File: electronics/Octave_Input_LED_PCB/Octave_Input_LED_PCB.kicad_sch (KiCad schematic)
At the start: 58 parts, among them J1 HRO_TYPE-C-31-M-12, J2 Conn_01x12, J3 Conn_01x12, SW1 SW_Hot_Swap_Socket, SW10 SW_Hot_Swap_Socket, SW11 SW_Hot_Swap_Socket, SW12 SW_Hot_Swap_Socket, SW2 SW_Hot_Swap_Socket, SW21 Alps_Alpine_SKRP, SW22 Alps_Alpine_SKRP, SW3 SW_Hot_Swap_Socket, SW4 SW_Hot_Swap_Socket, SW5 SW_Hot_Swap_Socket, SW6 SW_Hot_Swap_Socket, SW7 SW_Hot_Swap_Socket, SW8 SW_Hot_Swap_Socket, SW9 SW_Hot_Swap_Socket, U1 AP2112K-3.3, U2 Raspberry_Pi_RP2040, U3 W25Q64JVSS, Y1 12MHz

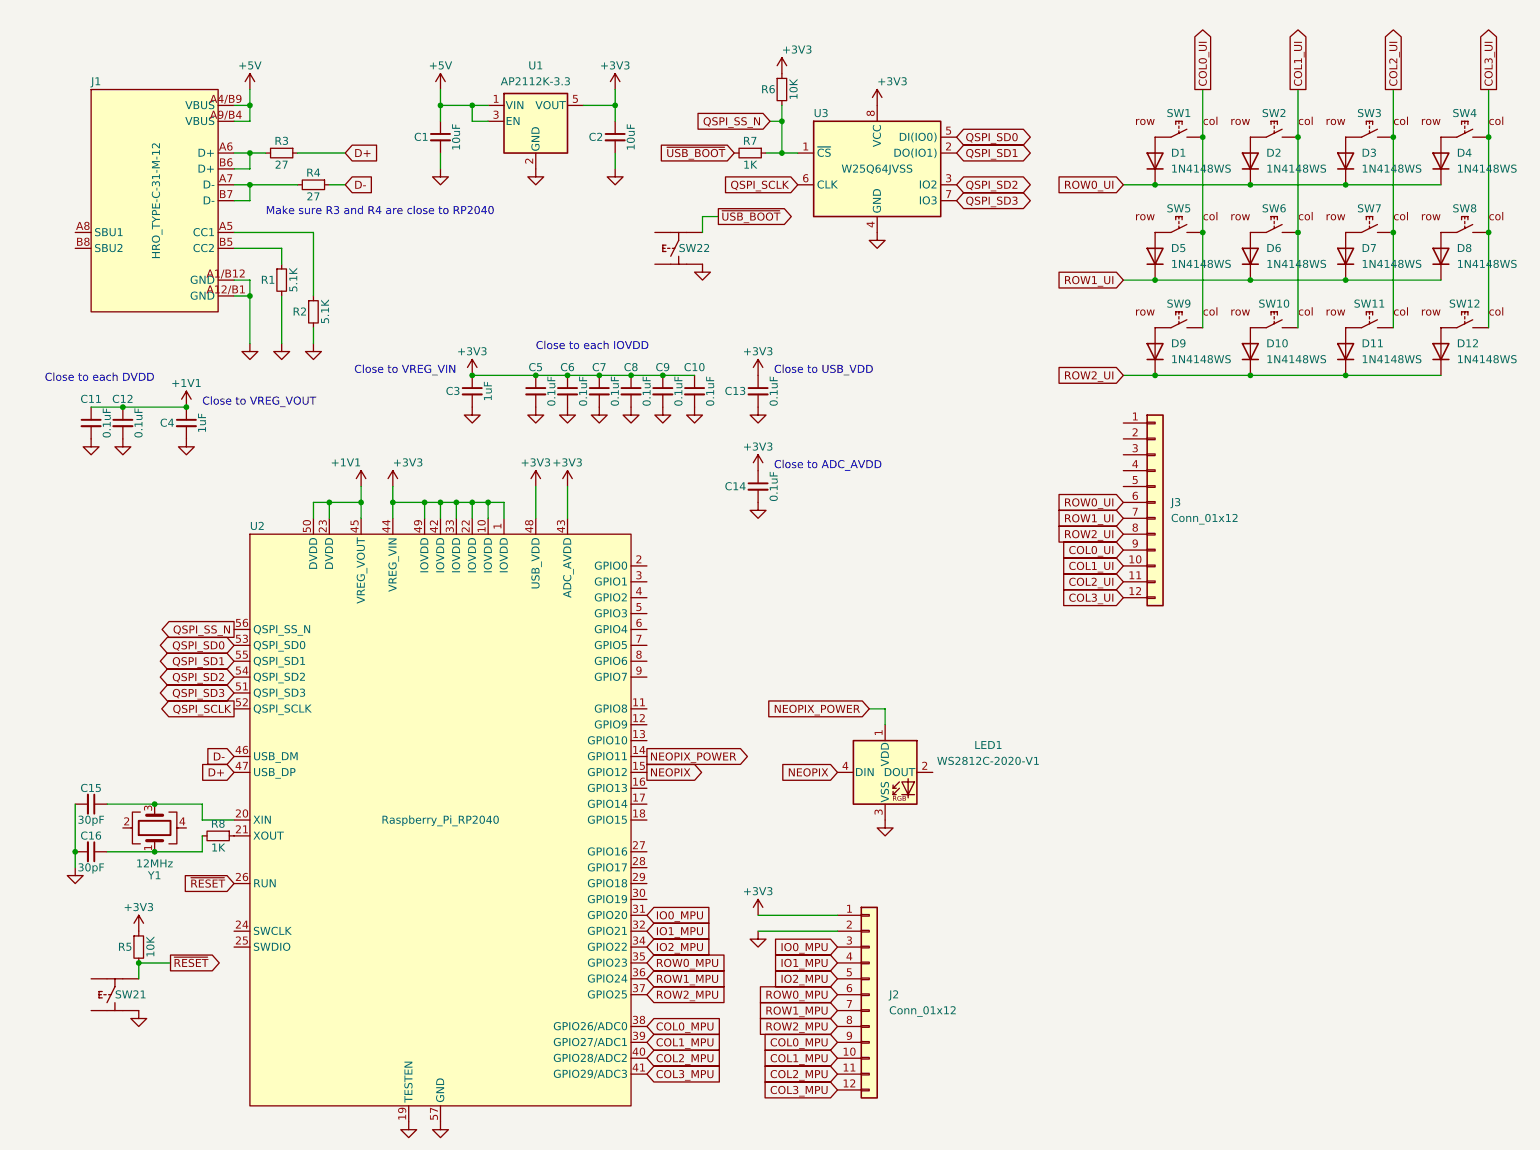
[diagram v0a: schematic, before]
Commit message: Remove CPU PCB from Input LED PCB
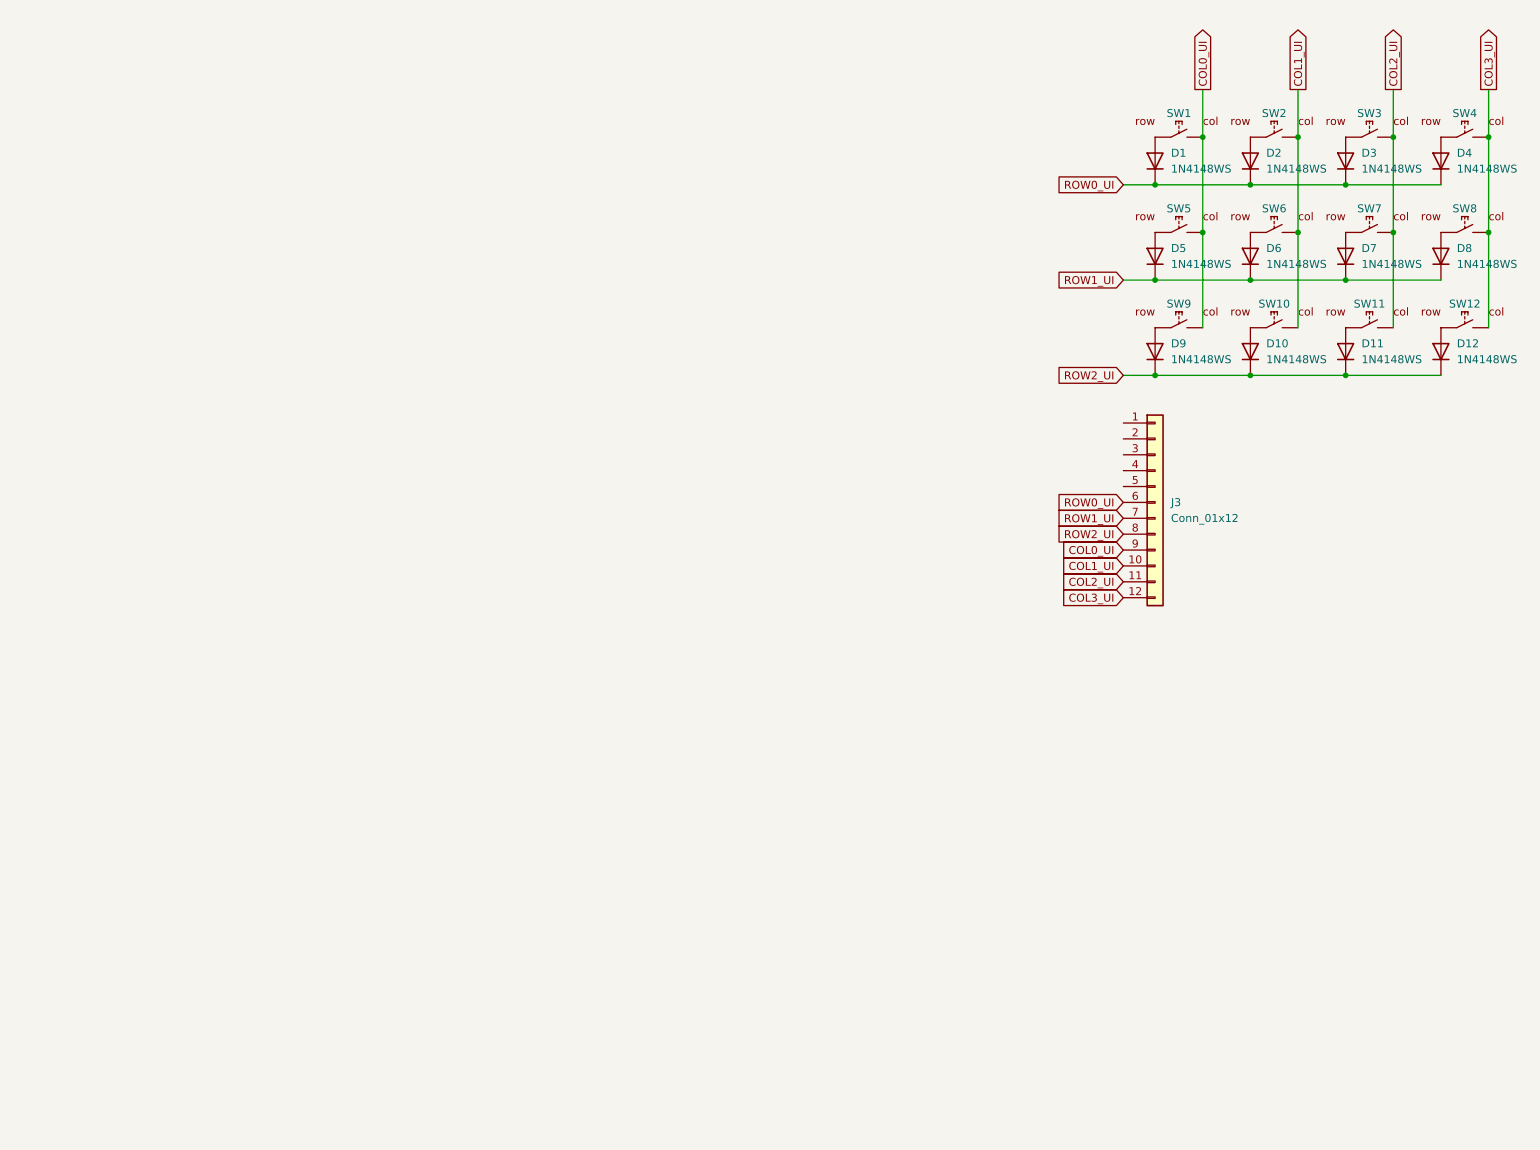
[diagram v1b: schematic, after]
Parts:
- removed C1, C2: 10uF, Capacitor_SMD:C_0402_1005Metric, symbol Device:C_Small
- removed C10, C11, C12, C13, C14, C5, C6, C7, C8, C9: 0.1uF, Capacitor_SMD:C_0402_1005Metric, symbol Device:C_Small
- removed C15, C16: 30pF, Capacitor_SMD:C_0402_1005Metric, symbol Device:C_Small
- removed C3, C4: 1uF, Capacitor_SMD:C_0402_1005Metric, symbol Device:C_Small
- removed J1: HRO_TYPE-C-31-M-12, Octave_Library:HRO_TYPE-C-31-M-12, symbol Octave_Library:HRO_TYPE-C-31-M-12
- removed J2: Conn_01x12, Octave_Library:JUSHUO_AFC01-S12FCC-00, symbol Connector_Generic:Conn_01x12
- removed LED1: WS2812C-2020-V1, Octave_Library:WS2812C-2020, symbol LED:WS2812B
- removed R1, R2: 5.1K, Resistor_SMD:R_0402_1005Metric, symbol Device:R_Small
- removed R3, R4: 27, Resistor_SMD:R_0402_1005Metric, symbol Device:R_Small
- removed R5, R6: 10K, Resistor_SMD:R_0402_1005Metric, symbol Device:R_Small
- removed R7, R8: 1K, Resistor_SMD:R_0402_1005Metric, symbol Device:R_Small
- removed SW21, SW22: Alps_Alpine_SKRP, Octave_Library:Tactile_Switch_SKRP_Series, symbol Octave_Library:Alps_Alpine_SKRP
- removed U1: AP2112K-3.3, Package_TO_SOT_SMD:SOT-23-5, symbol Regulator_Linear:AP2112K-3.3
- removed U2: Raspberry_Pi_RP2040, Octave_Library:RP2040_QFN-56, symbol Octave_Library:Raspberry_Pi_RP2040
- removed U3: W25Q64JVSS, Package_SO:SOIC-8_5.23x5.23mm_P1.27mm, symbol Memory_Flash:W25Q32JVSS
- removed Y1: 12MHz, Crystal:Crystal_SMD_3225-4Pin_3.2x2.5mm, symbol Device:Crystal_GND24
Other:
- note removed: "Close to ADC_AVDD"
- note removed: "Close to USB_VDD"
- note removed: "Close to VREG_VIN"
- note removed: "Close to VREG_VOUT"
- note removed: "Close to each DVDD"
- note removed: "Close to each IOVDD"
- note removed: "Make sure R3 and R4 are close to RP2040"

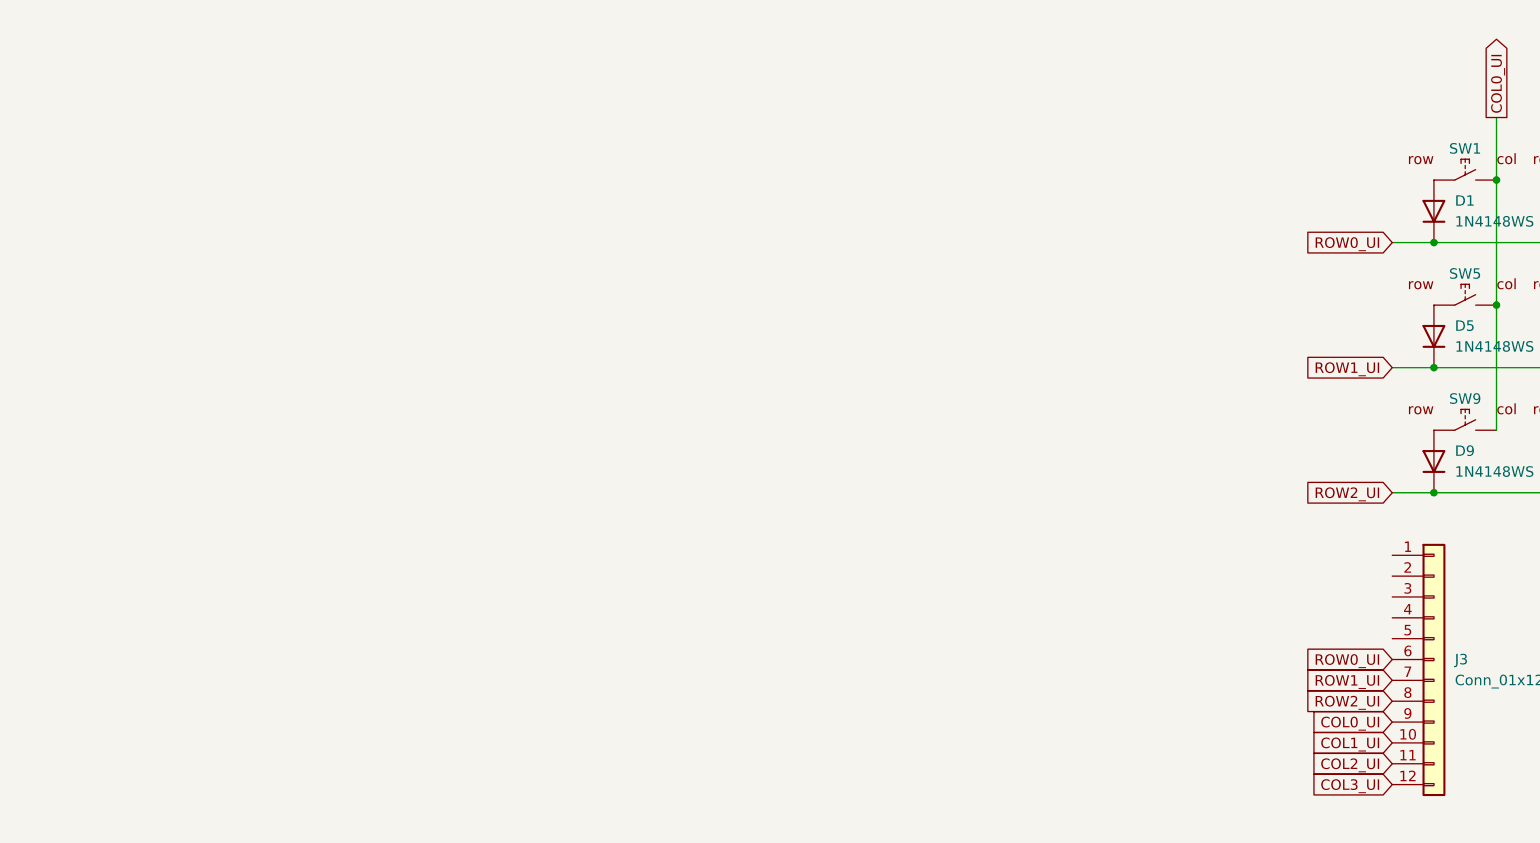
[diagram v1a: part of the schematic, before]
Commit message: Add footprint of WS2812B-Mini with inverted placement
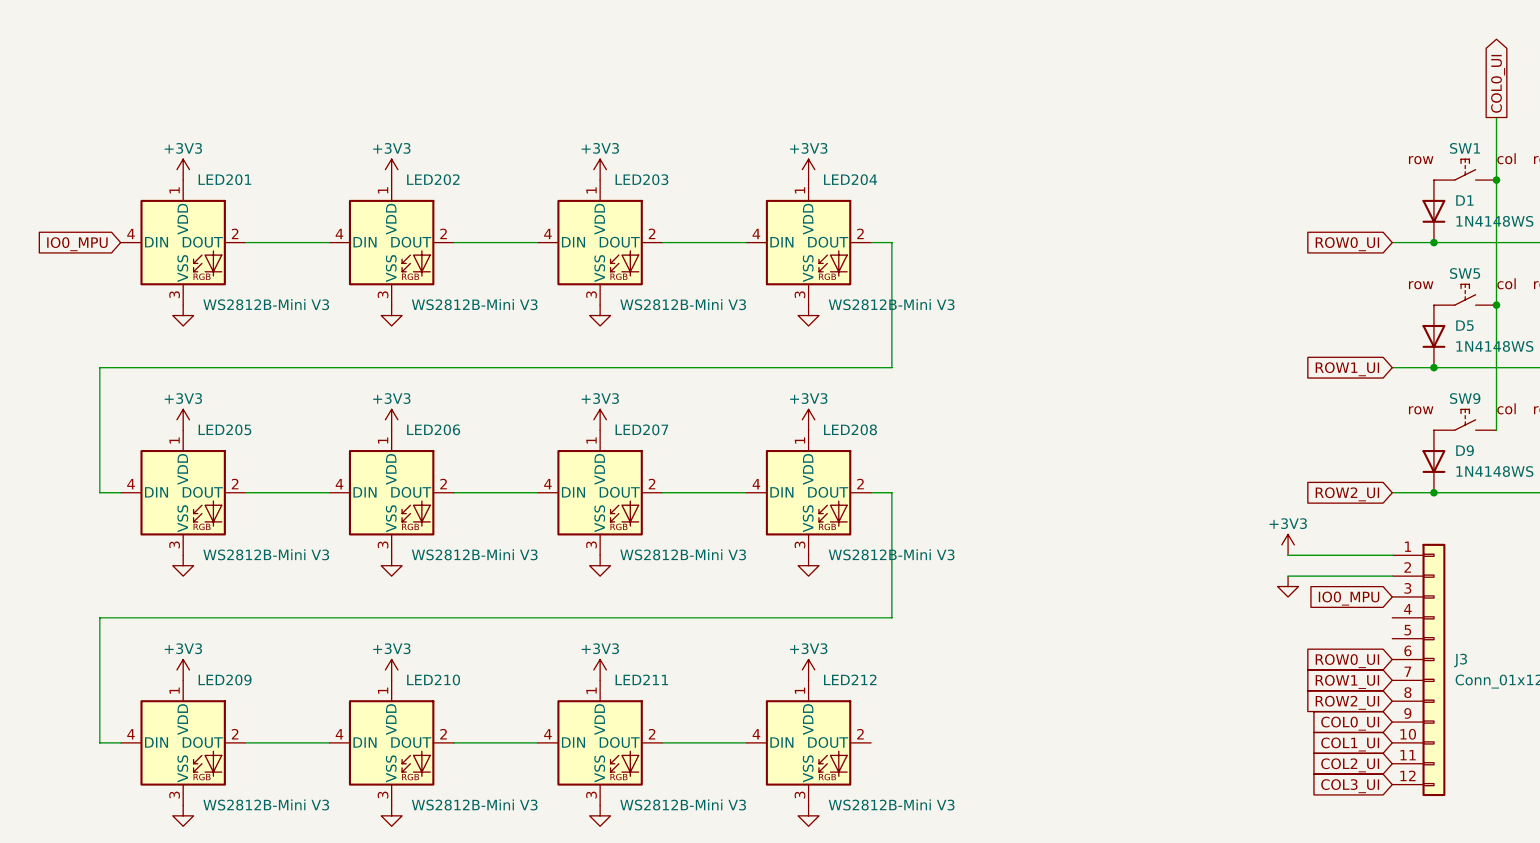
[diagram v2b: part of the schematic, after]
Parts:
- added LED201, LED202, LED203, LED204, LED205, LED206, LED207, LED208, LED209, LED210, LED211, LED212: WS2812B-Mini V3, Octave_Library:WS2812B-Mini_Inverted, symbol LED:WS2812B
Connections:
- net +3V3: now reaches J3.1 (Pin_1)
- net +3V3: now also LED201.1 (VDD), LED202.1 (VDD), LED203.1 (VDD), LED204.1 (VDD), LED205.1 (VDD), LED206.1 (VDD), LED207.1 (VDD), LED208.1 (VDD), LED209.1 (VDD), LED210.1 (VDD), LED211.1 (VDD), LED212.1 (VDD)
- net GND: now reaches J3.2 (Pin_2)
- net GND: now also LED201.3 (VSS), LED202.3 (VSS), LED203.3 (VSS), LED204.3 (VSS), LED205.3 (VSS), LED206.3 (VSS), LED207.3 (VSS), LED208.3 (VSS), LED209.3 (VSS), LED210.3 (VSS), LED211.3 (VSS), LED212.3 (VSS)
- net IO0_MPU: now reaches J3.3 (Pin_3)
- net IO0_MPU: now also LED201.4 (DIN)
- new net: LED211.2 (DOUT), LED212.4 (DIN)
- new net: LED210.2 (DOUT), LED211.4 (DIN)
- new net: LED209.2 (DOUT), LED210.4 (DIN)
- new net: LED202.2 (DOUT), LED203.4 (DIN)
- new net: LED201.2 (DOUT), LED202.4 (DIN)
- new net: LED205.2 (DOUT), LED206.4 (DIN)
- new net: LED204.2 (DOUT), LED205.4 (DIN)
- new net: LED203.2 (DOUT), LED204.4 (DIN)
- new net: LED208.2 (DOUT), LED209.4 (DIN)
- new net: LED207.2 (DOUT), LED208.4 (DIN)
- new net: LED206.2 (DOUT), LED207.4 (DIN)
